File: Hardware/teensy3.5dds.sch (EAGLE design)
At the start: 78 parts, among them IC1 AD8034ARZ, IC2 AD8034ARZ, IC3 AD8034ARZ, IC4 AD8034ARZ, IC5 AD8034ARZ, IC6 AD8034ARZ, IC7 AD8034ARZ, J1 1776275-2, J2 1776275-2, Q1 CSM-7X-DU, X1 1-227161-0

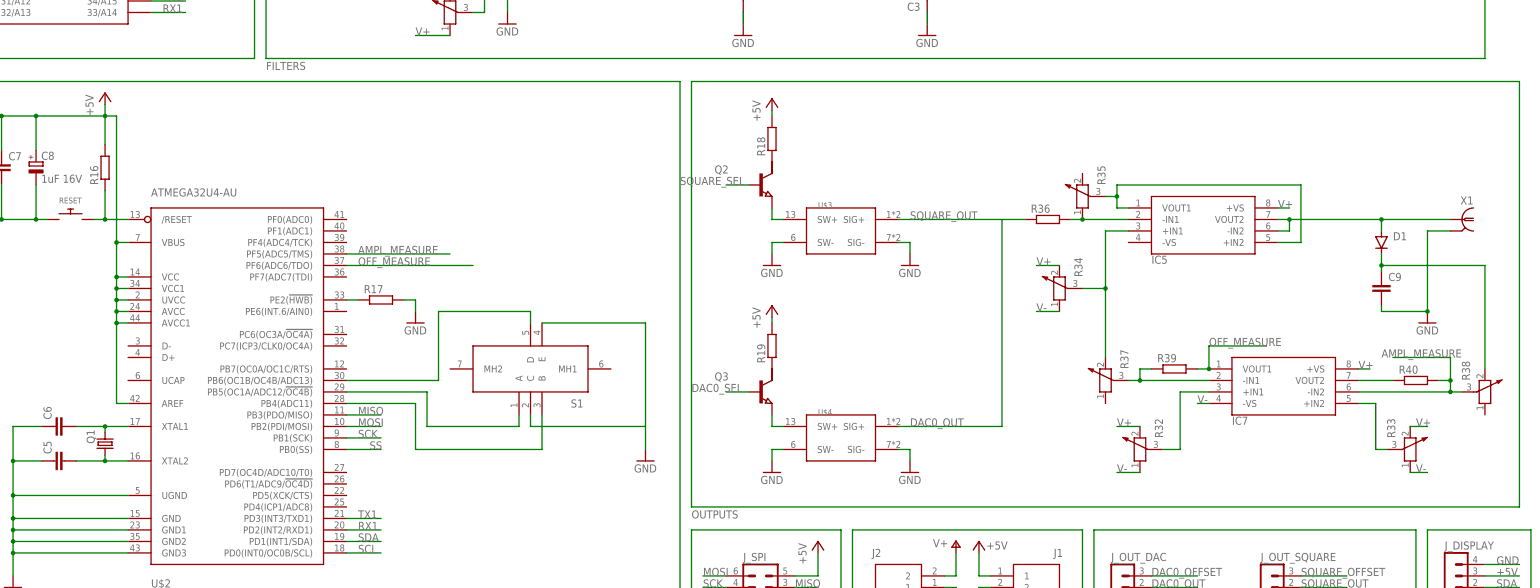
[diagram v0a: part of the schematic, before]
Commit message: hardware: better output select circuit And start arranging the components on the board
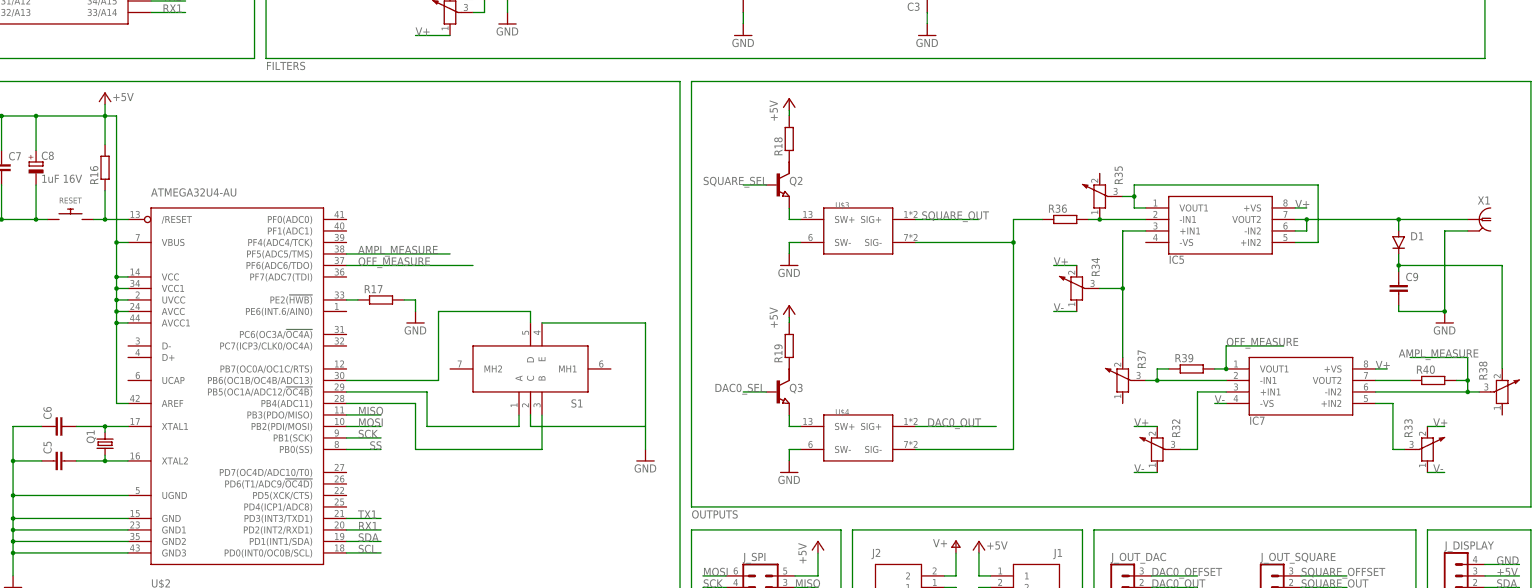
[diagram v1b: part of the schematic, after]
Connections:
- new net N$37: R36.1, U$3.SIG-, U$4.SIG-
- net GND: no longer U$3.SIG-, U$4.SIG-
- net SQUARE_OUT: no longer R36.1
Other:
- moved on the sheet: C9, D1, IC5, IC7, Q2, Q3, R18, R19, R32, R33, R34, R35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

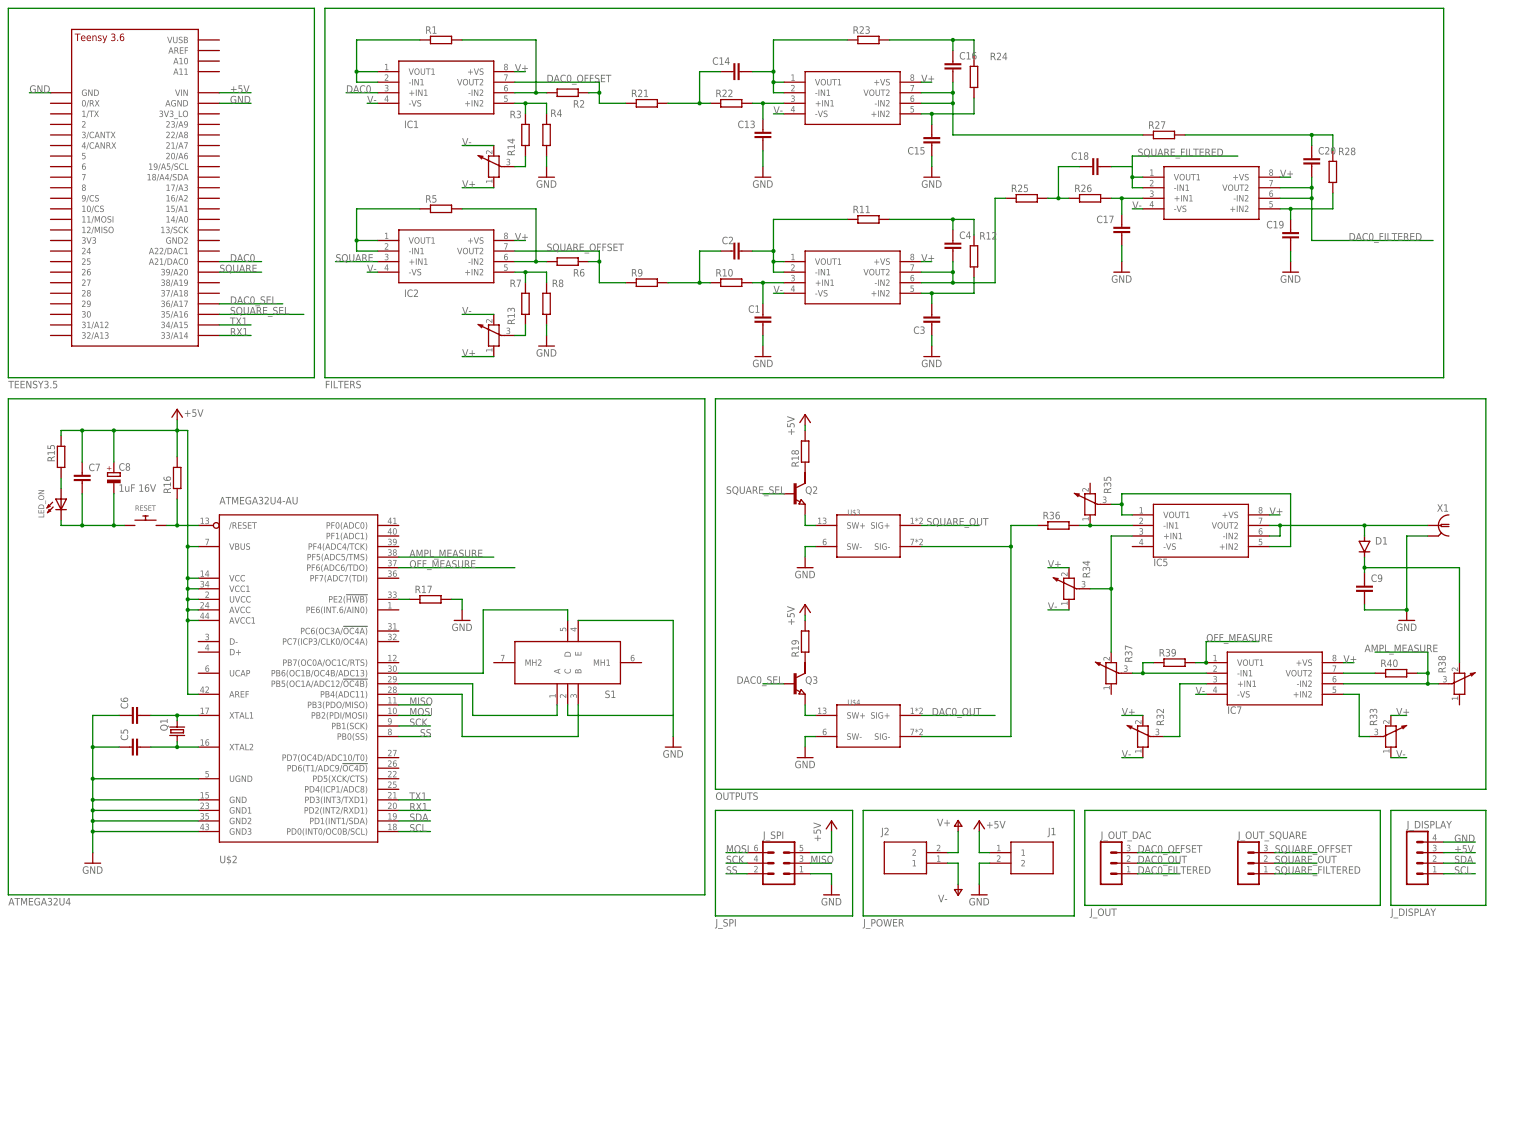
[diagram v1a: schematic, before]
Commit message: hardware: switch to electronic opamp symbol * Add decoupling caps for each opamp IC * Change place to peak detector circuit, although the whole circuit needs to be changed
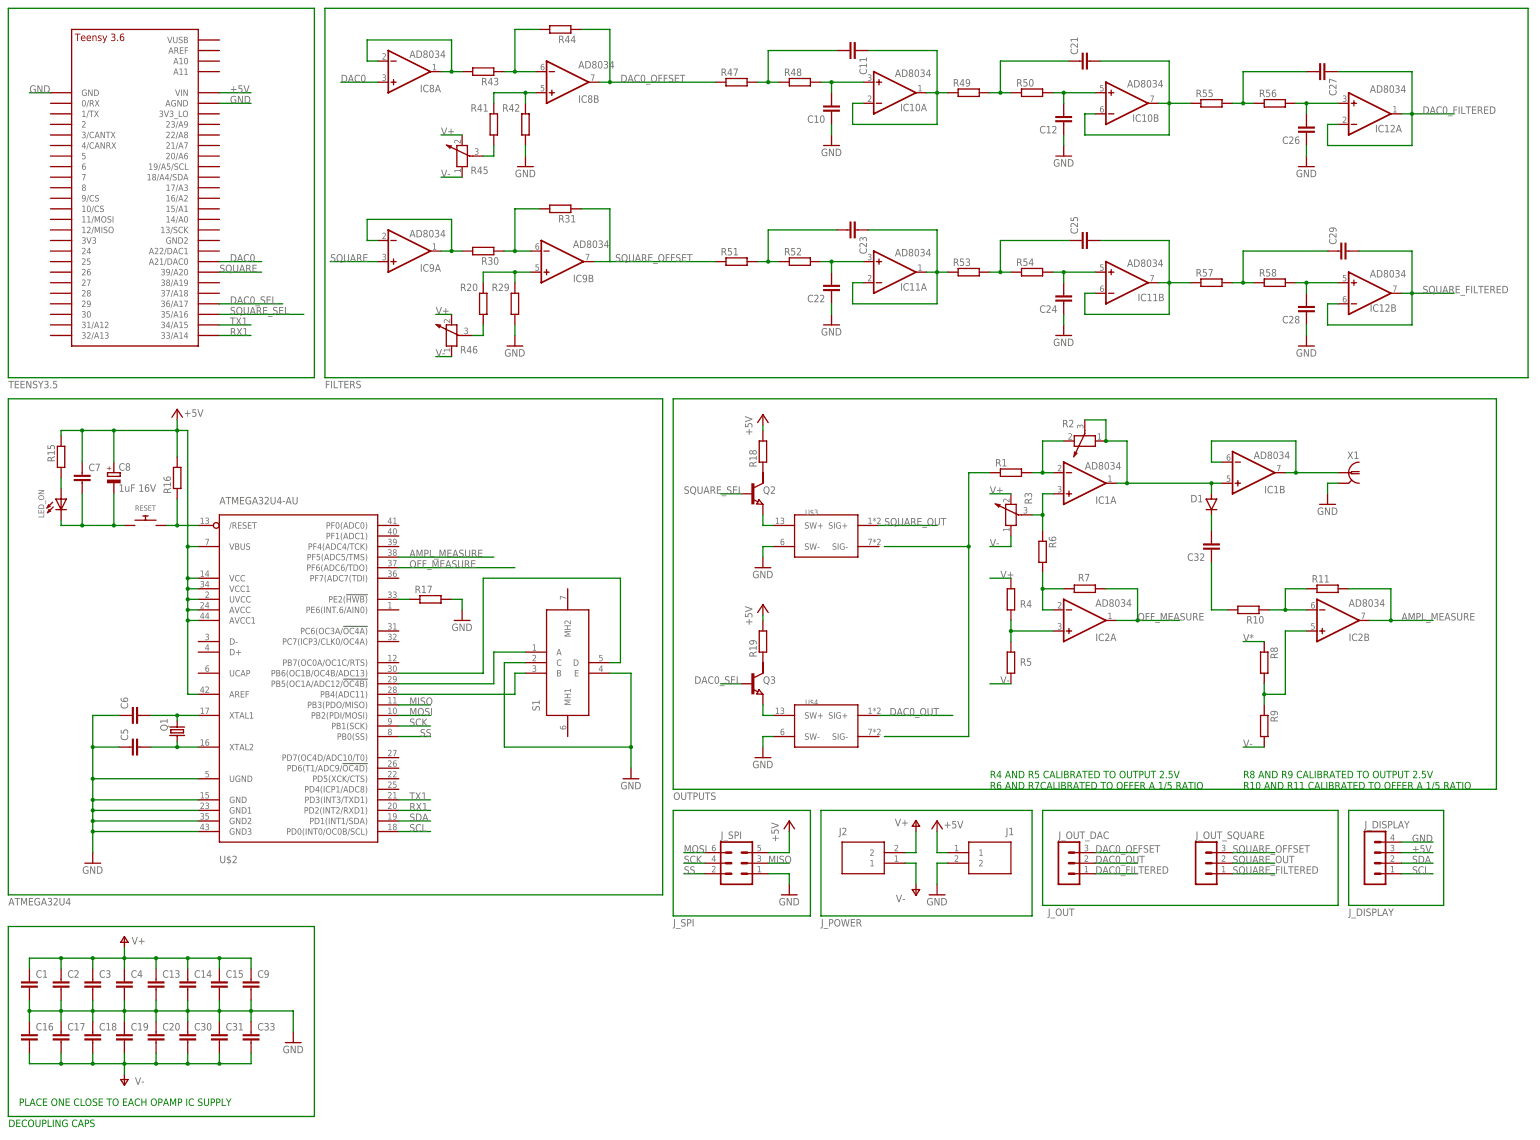
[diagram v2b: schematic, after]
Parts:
- removed IC3, IC4, IC5, IC6, IC7: AD8034ARZ, AD8034ARZ:AD8034ARZ
- removed R12, R21, R22, R23, R24, R25, R26, R27, R28: (no value), rcl:R-EU_M0805
- removed R13, R14, R32, R33, R34, R35, R37, R38: (no value), rcl:POTENTIOMETER_PT-10
- removed R36, R39, R40: (no value), rcl:R-EU_R0805
- added C10, C11, C12, C21, C22, C23, C24, C25, C26, C27, C28, C29, C30, C31, C32, C33: (no value), rcl:C-EUC0805
- added IC10, IC11, IC12, IC8, IC9: AD8034, linear:TL082D
- added R20, R29, R30, R31, R41, R42, R43, R44, R47, R48, R51, R52, R55, R56: (no value), rcl:R-EU_R0805
- added R45, R46: (no value), rcl:POTENTIOMETER_PT-10
- added R49, R50, R53, R54, R57, R58: (no value), rcl:R-EU_M0805
- C1, C13, C14, C15, C16, C17, C18, C19, C2, C20, C3, C4: device rcl:C-EUC0805K -> rcl:C-EUC0805
- IC1, IC2: value AD8034ARZ -> AD8034; device AD8034ARZ:AD8034ARZ -> linear:TL082D
- R1, R10, R11, R4, R5, R6, R7, R8, R9: device rcl:R-EU_M0805 -> rcl:R-EU_R0805
- R2, R3: device rcl:R-EU_M0805 -> rcl:POTENTIOMETER_PT-10
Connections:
- removed net N$12: R13.3, R7.1
- removed net N$17: C4.1, R11.2, R12.1
- removed net N$18: C13.1, IC3.+IN1, R22.2
- removed net N$19: C14.2, IC3.-IN1, IC3.VOUT1, R23.1
- removed net N$2: IC1.-IN1, IC1.VOUT1, R1.1
- removed net N$20: C14.1, R21.2, R22.1
- removed net N$21: C16.2, IC3.-IN2, IC3.VOUT2, R27.1
- removed net N$23: C16.1, R23.2, R24.1
- removed net N$24: C17.1, IC4.+IN1, R26.2
- removed net N$26: C18.1, R25.2, R26.1
- removed net N$27: S1.C
- removed net N$28: C19.2, IC4.+IN2, R28.2
- removed net N$29: C20.1, R27.2, R28.1
- removed net N$37: R36.1, U$3.SIG-, U$4.SIG-
- removed net N$43: IC5.-IN1, R35.1, R36.2
- removed net N$44: IC5.+IN2, IC5.VOUT1, R35.3
- removed net N$45: IC5.+IN1, R34.3, R37.2
- removed net N$46: IC7.-IN1, R37.3, R39.1
- removed net N$47: D1.A, IC5.-IN2, IC5.VOUT2, X1.1
- removed net N$48: IC7.+IN2, R33.3
- removed net N$49: IC7.+IN1, R32.3
- removed net N$52: C9.1, D1.C, R38.2
- removed net N$55: IC7.VOUT2, R40.1
- removed net N$7: IC1.+IN2, R3.2, R4.2
- new net N$38: IC9A.-IN, IC9A.OUT, R30.2
- new net N$41: IC8A.-IN, IC8A.OUT, R43.2
- new net N$50: C11.2, R47.2, R48.1
- new net N$51: IC8B.-IN, R43.1, R44.2
- new net N$53: C11.1, IC10A.-IN, IC10A.OUT, R49.1
- new net N$54: IC8B.+IN, R41.2, R42.2
- new net N$56: R41.1, R45.3
- new net N$57: IC9B.-IN, R30.1, R31.2
- new net N$58: C10.2, IC10A.+IN, R48.2
- new net N$59: IC9B.+IN, R20.2, R29.2
- new net N$60: R20.1, R46.3
- new net N$61: C21.1, R49.2, R50.1
- new net N$62: C21.2, IC10B.-IN, IC10B.OUT, R55.1
- new net N$63: C12.2, IC10B.+IN, R50.2
- new net N$66: C23.2, R51.2, R52.1
- new net N$67: C23.1, IC11A.-IN, IC11A.OUT, R53.1
- new net N$68: C22.2, IC11A.+IN, R52.2
- new net N$69: C25.1, R53.2, R54.1
- new net N$70: C25.2, IC11B.-IN, IC11B.OUT, R57.1
- new net N$71: C24.2, IC11B.+IN, R54.2
- new net N$73: C27.2, R55.2, R56.1
- new net N$75: C26.2, IC12A.+IN, R56.2
- new net N$76: C29.1, R57.2, R58.1
- new net N$78: C28.2, IC12B.+IN, R58.2
- new net V*: R8.1
- net AMPL_MEASURE: now also IC2B.OUT, R11.2; no longer IC7.-IN2, R38.3, R40.2
- net DAC0: now also IC8A.+IN; no longer IC1.+IN1
- net DAC0_FILTERED: now also C27.1, IC12A.-IN, IC12A.OUT; no longer C20.2, IC4.-IN2, IC4.VOUT2
- net DAC0_OFFSET: now also IC8B.OUT, R44.1, R47.1; no longer IC1.VOUT2, R2.2, R21.1
- net GND: now also C10.1, C12.1, C14.2, C15.2, C16.1, C17.1, C18.1, C2.2, C20.1, C22.1, C24.1, C26.1, C28.1, C3.2, C30.1, C31.1, C33.1, C4.2, R29.1, R42.1, S1.C; no longer C15.1, C17.2, C3.1, R4.1, R8.1
- net N$10: now also R1.1; no longer IC2.-IN2, R5.2, R6.1
- net N$11: now also IC2A.-IN, R6.2, R7.2; no longer C1.1, IC6.+IN1, R10.2
- net N$13: now also IC2A.+IN, R4.1, R5.2; no longer IC2.+IN2, R7.2, R8.2
- net N$14: now also C32.2, D1.C; no longer C2.2, IC6.-IN1, IC6.VOUT1, R11.1
- net N$15: now also C32.1, R10.2; no longer C4.2, IC6.-IN2, IC6.VOUT2, R25.1
- net N$16: now also IC2B.-IN, R10.1, R11.1; no longer C3.2, IC6.+IN2, R12.2
- net N$22: now also IC2B.+IN, R8.2, R9.1; no longer C15.2, IC3.+IN2, R24.2
- net N$3: now also IC1A.+IN, R3.3, R6.1; no longer IC1.-IN2, R1.2, R2.1
- net N$5: now also IC1A.-IN, R1.2, R2.2; no longer C2.1, R10.1, R9.2
- net N$6: now also IC1B.-IN, IC1B.OUT, X1.1; no longer R14.3, R3.1
- net N$9: now also D1.A, IC1A.OUT, IC1B.+IN, R2.1, R2.3; no longer IC2.-IN1, IC2.VOUT1, R5.1
- net OFF_MEASURE: now also IC2A.OUT, R7.1; no longer IC7.VOUT1, R39.2
- net SQUARE: now also IC9A.+IN; no longer IC2.+IN1
- net SQUARE_FILTERED: now also C29.2, IC12B.-IN, IC12B.OUT; no longer C18.2, IC4.-IN1, IC4.VOUT1
- net SQUARE_OFFSET: now also IC9B.OUT, R31.1, R51.1; no longer IC2.VOUT2, R6.2, R9.1
- net V+: now also C1.1, C13.1, C14.1, C15.1, C2.1, C3.1, C4.1, C9.1, R3.2, R4.2, R45.2, R46.2; no longer IC1.+VS, IC2.+VS, IC3.+VS, IC4.+VS, IC5.+VS, IC6.+VS, IC7.+VS, R13.1, R14.1, R32.2, R33.2, R34.2
- net V-: now also C16.2, C17.2, C18.2, C19.2, C20.2, C30.2, C31.2, C33.2, R3.1, R45.1, R46.1, R5.1, R9.2; no longer IC1.-VS, IC2.-VS, IC3.-VS, IC4.-VS, IC6.-VS, IC7.-VS, R13.2, R14.2, R32.1, R33.1, R34.1
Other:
- note added: "DECOUPLING CAPS"
- note added: "PLACE ONE CLOSE TO EACH OPAMP IC SUPPLY"
- note added: "R4 AND R5 CALIBRATED TO OUTPUT 2.5V R6 AND R7CALIBRATED TO OFFER A 1/5 RATIO"
- note added: "R8 AND R9 CALIBRATED TO OUTPUT 2.5V R10 AND R11 CALIBRATED TO OFFER A 1/5 RATIO"
- moved on the sheet: C1, C13, C14, C15, C16, C17, C18, C19, C2, C20, C3, C4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

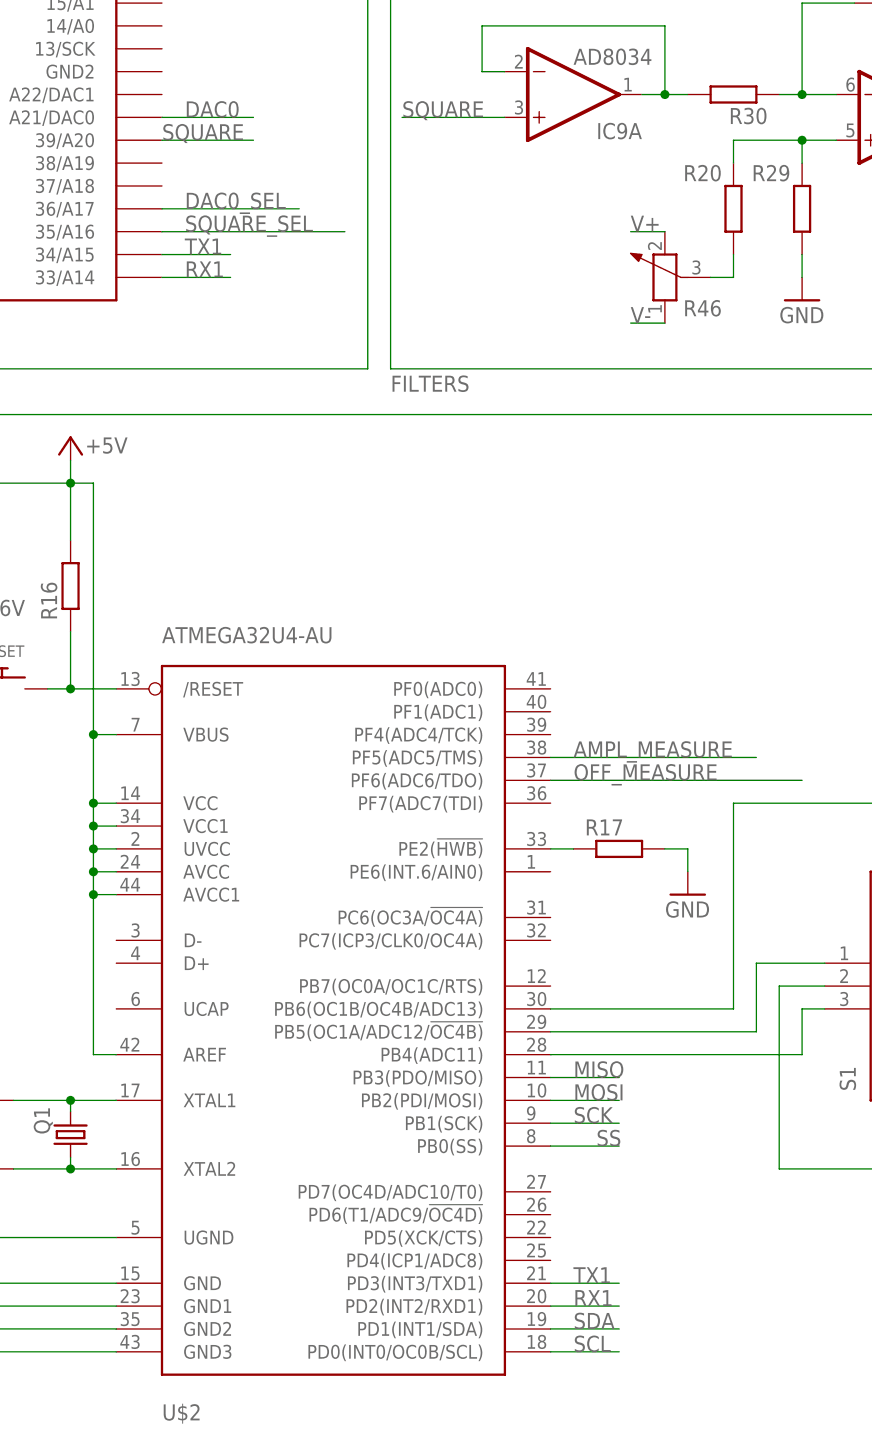
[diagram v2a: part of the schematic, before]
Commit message: hardware: add interrupt pin between 32u4 and teensy
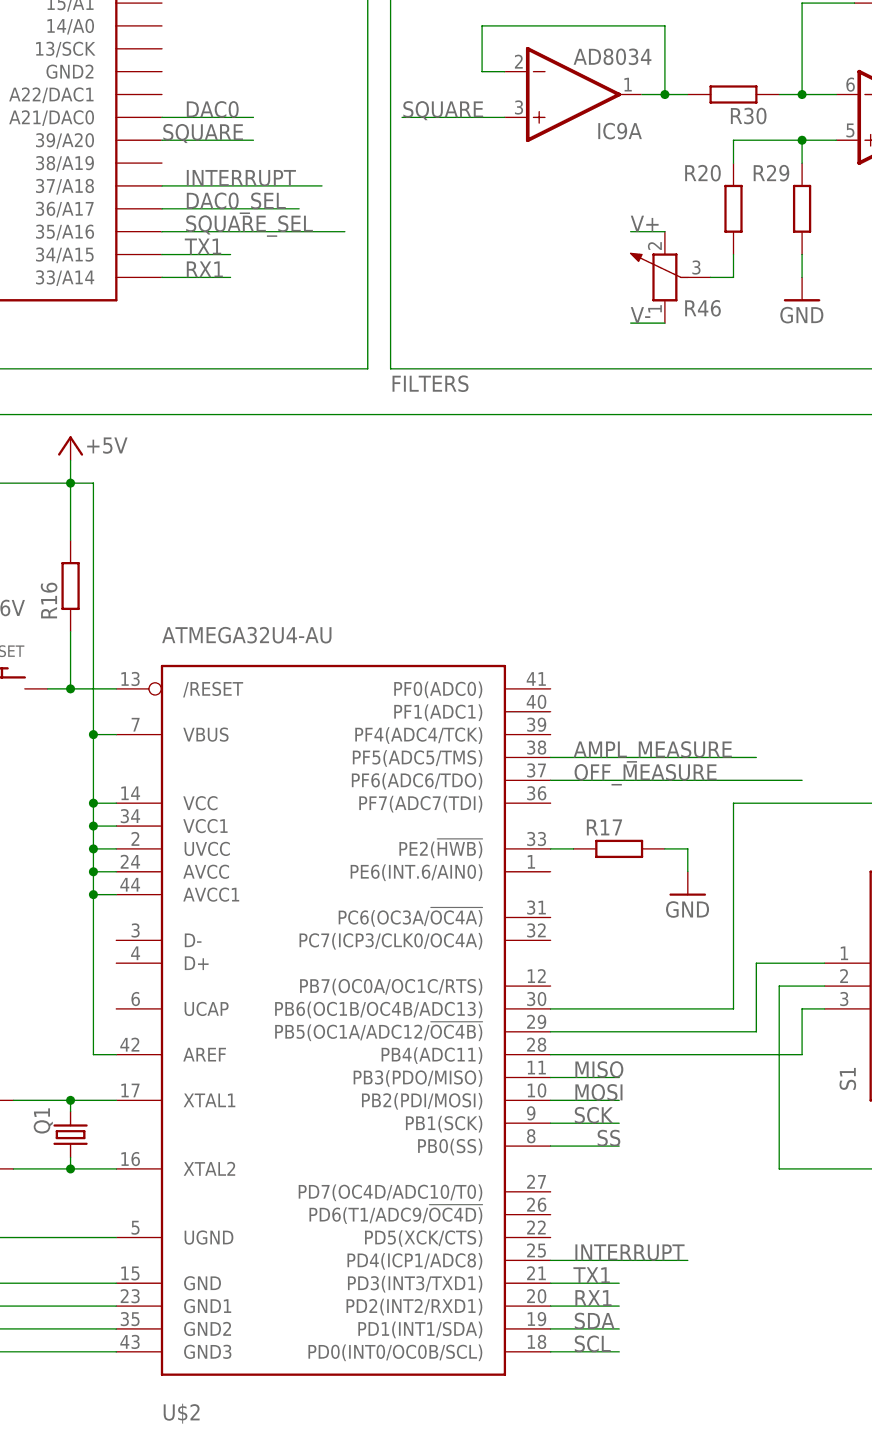
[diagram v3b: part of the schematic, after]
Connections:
- new net INTERRUPT: U$1.37/A18, U$2.PD4(ICP1/ADC8)
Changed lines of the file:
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@@
+</segment>
+</net>
+<net name="INTERRUPT" class="0">
+<segment>
+<pinref part="U$2" gate="G$1" pin="PD4(ICP1/ADC8)"/>
+<wire x1="63.5" y1="-154.94" x2="78.74" y2="-154.94" width="0.1524" layer="91"/>
+<label x="66.04" y="-154.94" size="1.778" layer="95"/>
+</segment>
+<segment>
+<pinref part="U$1" gate="G$1" pin="37/A18"/>
+<wire x1="20.32" y1="-35.56" x2="38.1" y2="-35.56" width="0.1524" layer="91"/>
+<label x="22.86" y="-35.56" size="1.778" layer="95"/>
 </segment>
 </net>
